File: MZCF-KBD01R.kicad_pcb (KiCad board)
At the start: 2 copper layers, 256.5 x 127.8 mm, 126 parts, among them CN2 XH-4AW_C2908613, SW1 SW_Push, SW10 SW_Push, SW11 SW_Push, SW12 SW_Push, SW13 SW_Push, SW14 SW_Push, SW15 SW_Push, SW16 SW_Push, SW17 SW_Push, SW18 SW_Push, SW19 SW_Push, SW2 SW_Push, SW20 SW_Push, SW21 SW_Push, SW22 SW_Push, SW23 SW_Push, SW24 SW_Push, SW25 SW_Push, SW26 SW_Push, SW27 SW_Push, SW28 SW_Push, SW29 SW_Push, SW3 SW_Push, SW30 SW_Push, SW31 SW_Push, SW32 SW_Push, SW33 SW_Push, SW34 SW_Push, SW35 SW_Push, SW36 SW_Push, SW37 SW_Push, SW38 SW_Push, SW39 SW_Push, SW4 SW_Push, SW40 SW_Push, SW41 SW_Push, SW42 SW_Push, SW43 SW_Push, SW44 SW_Push, SW45 SW_Push, SW46 SW_Push, SW47 SW_Push, SW48 SW_Push, SW49 SW_Push, SW5 SW_Push, SW50 SW_Push, SW51 SW_Push, SW52 SW_Push, SW53 SW_Push, SW55 SW_Push, SW56 SW_Push, SW6 SW_Push, SW7 SW_Push, SW8 SW_Push, SW9 SW_Push, U1 RP2040-ZERO

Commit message: feat: add hotswap MX switches and PCB stabilizer support
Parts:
- removed CN2: XH-4AW_C2908613, lcsc_footprints:C2908613_CONN-TH_XH-4AW
- removed D1, D12, D24, D35, D36, D40, D53, D55, D56: 1N4148W, ComboDiode
- removed the H1 at (22.4, 21.3)
- removed H10, H11, H12, H13, H2, H3, H4, H5, H6, H7, H8, H9: MountingHole_2.2mm_M2, MountingHole:MountingHole_2.2mm_M2
- removed SW1, SW12, SW24, SW35, SW36, SW40, SW53, SW55, SW56: SW_Push, MX
- added CN1: PJ-320A_C49284721, lcsc_footprints:C49284721_AUDIO-TH_PJ-320A_C49284721, B.Cu at (109.2, 28.5)
- added D54: 1N4148W, ComboDiode, B.Cu at (204.8, 140.3)
- added H1: MountingHole_2.2mm_M2, MountingHole:MountingHole_2.2mm_M2, F.Cu at (205.1, 116.2)
- added H1: MountingHole_2.2mm_M2, MountingHole:MountingHole_2.2mm_M2, F.Cu at (142.9, 87.0)
- added H1: MountingHole_2.2mm_M2, MountingHole:MountingHole_2.2mm_M2, F.Cu at (86.4, 134.0)
- added H1: MountingHole_2.2mm_M2, MountingHole:MountingHole_2.2mm_M2, F.Cu at (186.7, 44.5)
- added H1: MountingHole_2.2mm_M2, MountingHole:MountingHole_2.2mm_M2, F.Cu at (190.5, 76.2)
- added H1: MountingHole_2.2mm_M2, MountingHole:MountingHole_2.2mm_M2, F.Cu at (149.2, 142.9)
- added H1: MountingHole_2.2mm_M2, MountingHole:MountingHole_2.2mm_M2, F.Cu at (47.6, 22.9)
- added H1: MountingHole_2.2mm_M2, MountingHole:MountingHole_2.2mm_M2, F.Cu at (38.1, 67.9)
- added H1: MountingHole_2.2mm_M2, MountingHole:MountingHole_2.2mm_M2, F.Cu at (95.2, 67.9)
- added H1: MountingHole_2.2mm_M2, MountingHole:MountingHole_2.2mm_M2, F.Cu at (125.1, 44.5)
- added H1: MountingHole_2.2mm_M2, MountingHole:MountingHole_2.2mm_M2, F.Cu at (213.6, 21.6)
- added H1: MountingHole_2.2mm_M2, MountingHole:MountingHole_2.2mm_M2, F.Cu at (45.7, 144.1)
- added H1: MountingHole_2.2mm_M2, MountingHole:MountingHole_2.2mm_M2, F.Cu at (38.1, 44.5)
- added ST1: , STAB_MX, F.Cu at (171.4, 59.1)
- added ST2: , STAB_MX, F.Cu at (169.1, 97.2)
- added ST3: , STAB_MX, B.Cu at (157.2, 116.2)
- added ST4: , STAB_MX, F.Cu at (64.3, 135.3)
- added SW54: SW_Push, MX, F.Cu at (204.8, 135.3)
- moved D7 188.2 mm to (38.1, 35.5), turned to 0 degrees
- moved SW7 188.2 mm to (38.1, 30.5)
- moved U1 164.5 mm to (201.3, 33.0)
- moved D14 159.6 mm to (66.7, 64.1), turned to 0 degrees
- moved SW14 159.6 mm to (66.7, 59.1)
- moved D21 157.7 mm to (95.2, 83.1), turned to 0 degrees
- moved SW21 157.7 mm to (95.2, 78.1)
- moved D42 143.7 mm to (166.7, 140.3), turned to 0 degrees
- moved SW42 143.7 mm to (166.7, 135.3)
- moved D28 132.1 mm to (119.1, 102.2), turned to 0 degrees
- moved SW28 132.1 mm to (119.1, 97.2)
- moved D13 122.4 mm to (57.1, 35.5), turned to 0 degrees
- moved SW13 122.4 mm to (57.1, 30.5)
- moved D20 99.3 mm to (85.7, 64.1), turned to 0 degrees
- moved SW20 99.3 mm to (85.7, 59.1)
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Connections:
- D10 pad 1: /ROW2 -> /ROW3
- D11 pad 1: /ROW3 -> /ROW4
- D13 pad 1: /ROW5 -> /ROW0
- D14 pad 1: /ROW6 -> /ROW1
- D15 pad 1: /ROW0 -> /ROW2
- D16 pad 1: /ROW1 -> /ROW3
- D17 pad 1: /ROW2 -> /ROW4
- D18 pad 1: /ROW3 -> /ROW5
- D19 pad 1: /ROW4 -> /ROW0
- D20 pad 1: /ROW5 -> /ROW1
- D21 pad 1: /ROW6 -> /ROW2
- D22 pad 1: /ROW0 -> /ROW3
- D23 pad 1: /ROW1 -> /ROW4
- D25 pad 1: /ROW3 -> /ROW0
- D26 pad 1: /ROW4 -> /ROW1
- D27 pad 1: /ROW5 -> /ROW2
- D28 pad 1: /ROW6 -> /ROW3
- D29 pad 1: /ROW0 -> /ROW4
- D30 pad 1: /ROW1 -> /ROW5
- D31 pad 1: /ROW2 -> /ROW0
- D32 pad 1: /ROW3 -> /ROW1
- D33 pad 1: /ROW4 -> /ROW2
- D34 pad 1: /ROW5 -> /ROW3
- D37 pad 1: /ROW1 -> /ROW0
- D38 pad 1: /ROW2 -> /ROW1
- D39 pad 1: /ROW3 -> /ROW2
- D41 pad 1: /ROW5 -> /ROW4
- D42 pad 1: /ROW6 -> /ROW5
- D49 pad 1: /ROW6 -> /ROW0
- D50 pad 1: /ROW0 -> /ROW1
- D51 pad 1: /ROW1 -> /ROW2
- D52 pad 1: /ROW2 -> /ROW3
- D7 pad 1: /ROW6 -> /ROW0
- D8 pad 1: /ROW0 -> /ROW1
- D9 pad 1: /ROW1 -> /ROW2
- SW13 pad 1: /COL1 -> /COL2
- SW14 pad 1: /COL1 -> /COL2
- SW19 pad 1: /COL2 -> /COL3
- SW20 pad 1: /COL2 -> /COL3
- SW21 pad 1: /COL2 -> /COL3
- SW25 pad 1: /COL3 -> /COL4
- SW26 pad 1: /COL3 -> /COL4
- SW27 pad 1: /COL3 -> /COL4
- SW28 pad 1: /COL3 -> /COL4
- SW31 pad 1: /COL4 -> /COL5
- SW32 pad 1: /COL4 -> /COL5
- SW33 pad 1: /COL4 -> /COL5
- SW34 pad 1: /COL4 -> /COL5
- SW37 pad 1: /COL5 -> /COL6
- SW38 pad 1: /COL5 -> /COL6
- SW39 pad 1: /COL5 -> /COL6
- SW41 pad 1: /COL5 -> /COL6
- SW42 pad 1: /COL5 -> /COL6
- SW43 pad 1: /COL6 -> /COL7
- SW44 pad 1: /COL6 -> /COL7
- SW45 pad 1: /COL6 -> /COL7
- SW46 pad 1: /COL6 -> /COL7
- SW47 pad 1: /COL6 -> /COL7
- SW48 pad 1: /COL6 -> /COL7
- SW49 pad 1: /COL6 -> /COL8
- SW50 pad 1: /COL7 -> /COL8
- SW51 pad 1: /COL7 -> /COL8
- SW52 pad 1: /COL7 -> /COL8
- SW7 pad 1: /COL0 -> /COL1
- U1 pad 10: /ROW1 -> /ROW0
- U1 pad 11: /ROW2 -> /ROW1
- U1 pad 12: /ROW3 -> /ROW2
- U1 pad 13: /ROW4 -> /ROW3
- U1 pad 14: /ROW5 -> /ROW4
- U1 pad 15: /ROW6 -> /ROW5
- U1 pad 17: unconnected-(U1-GP26-Pad17) -> Net-(U1-GP26)
- U1 pad 18: unconnected-(U1-GP27-Pad18) -> Net-(U1-GP27)
- U1 pad 9: /ROW0 -> /COL8
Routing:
- net /ROW6: track 460.9 -> 0.00 mm, vias 1 -> 0
- net /COL5: track 561.0 -> 161.7 mm, vias 1 -> 0
- net /COL6: track 569.8 -> 186.5 mm, vias 1 -> 0
- net /COL7: track 509.1 -> 180.1 mm, vias 1 -> 0
- net /COL4: track 547.8 -> 235.3 mm, vias 2 -> 0
- net /COL3: track 542.7 -> 232.7 mm, vias 1 -> 0
- net /COL2: track 540.2 -> 273.7 mm, vias 2 -> 0
- net /COL8: track 0.00 -> 121.1 mm
- net /COL0: track 390.7 -> 296.6 mm, vias 1 -> 0
- net /COL1: track 353.7 -> 267.5 mm, vias 2 -> 0
- net /ROW5: track 358.7 -> 275.0 mm, vias 1 -> 0
- net Net-(U1-5V): track 85.4 -> 149.6 mm, vias 0 -> 1
- net /ROW4: track 317.9 -> 266.3 mm, vias 1 -> 2
- net Net-(U1-GP29): track 91.5 -> 142.4 mm
- net Net-(U1-GND): track 93.8 -> 144.4 mm, vias 0 -> 1
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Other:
- board size 256.5 x 127.8 mm -> 197.3 x 127.8 mm
- board text added: "MZCF-KBD01R V1 Rev.2"
- board text removed: "MZCF-KBD01R V1 Rev.1"

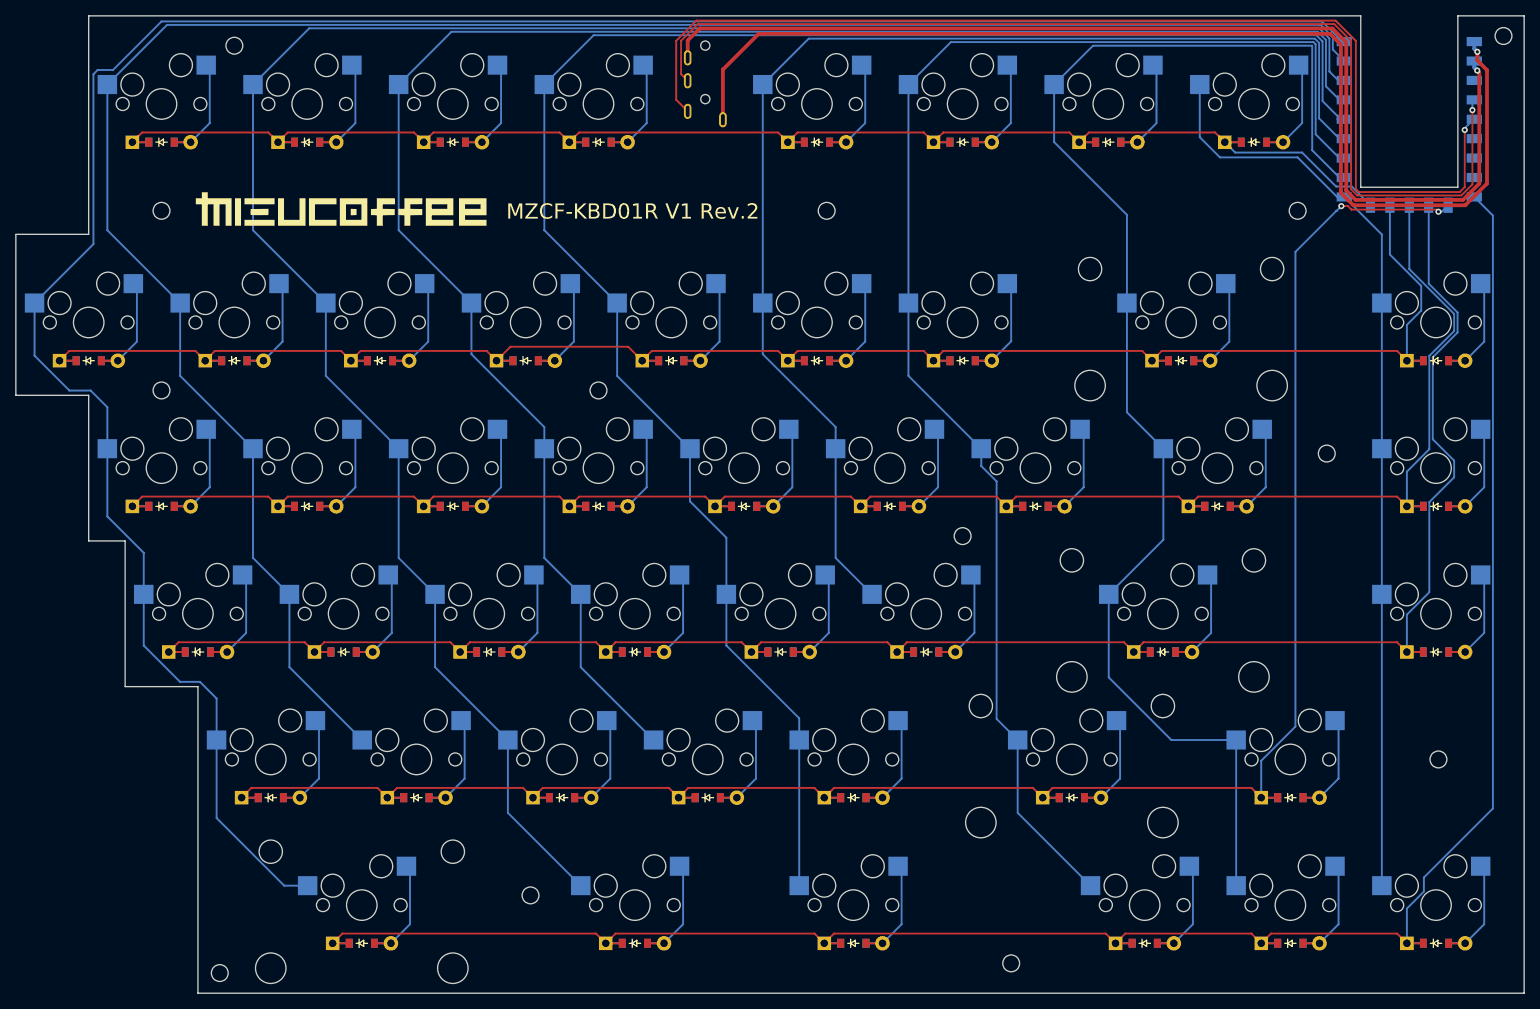
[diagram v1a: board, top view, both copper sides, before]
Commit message: fix(pcb): add controller cutouts and mating-edge clearance
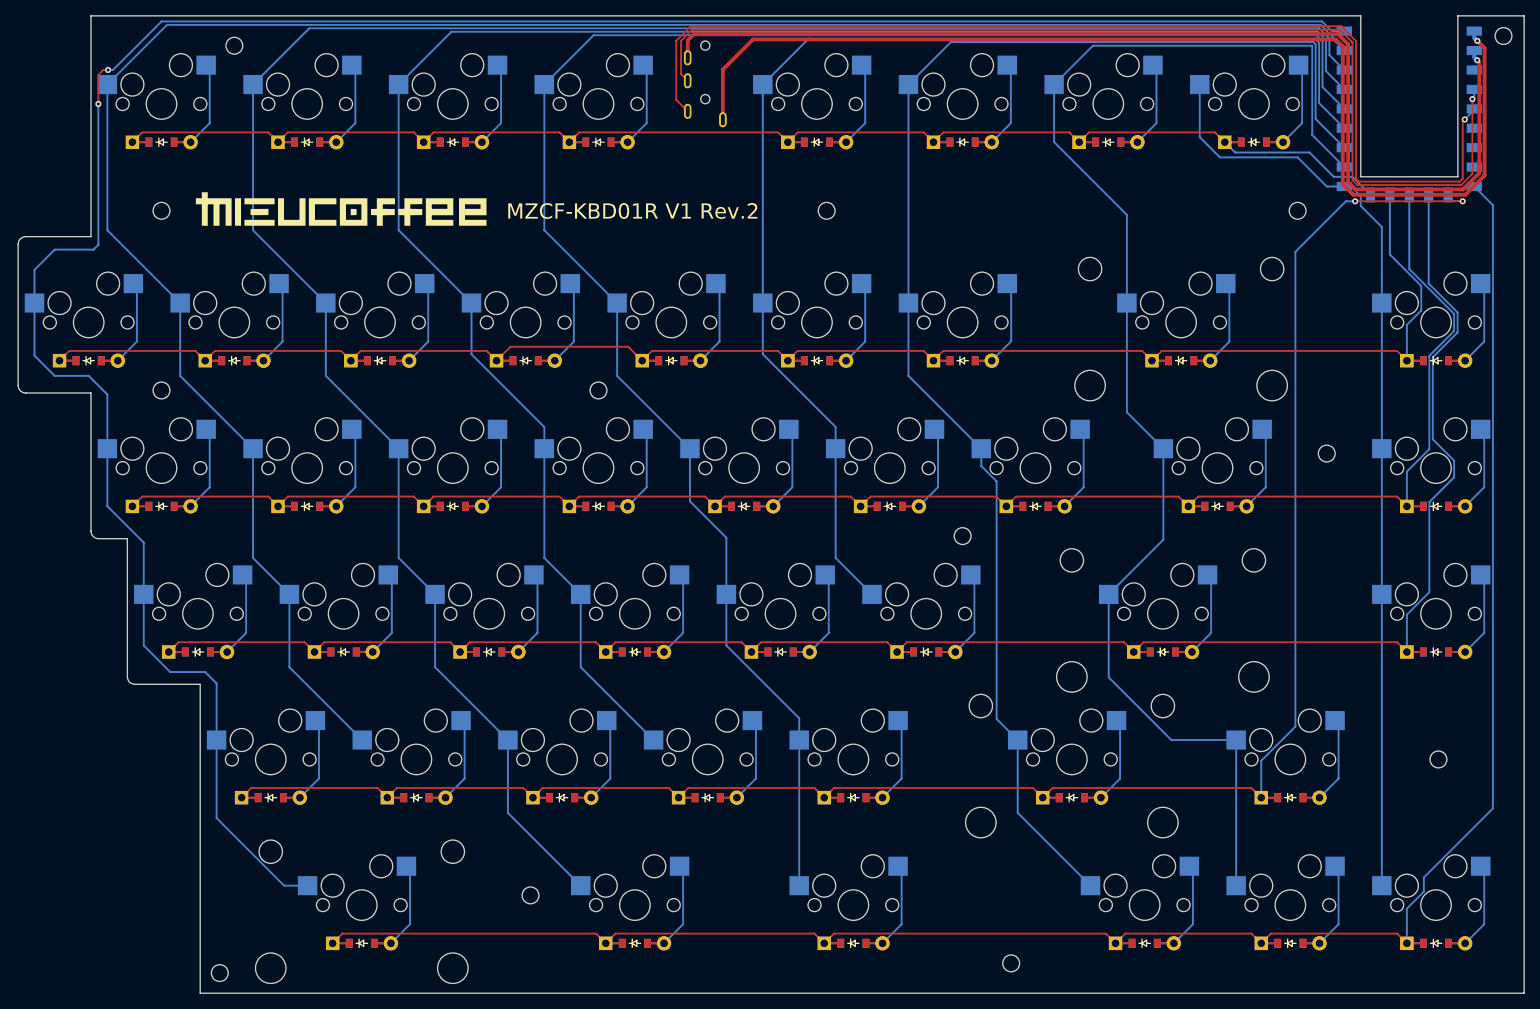
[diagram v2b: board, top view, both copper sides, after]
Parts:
- moved U1 1.37 mm to (201.3, 31.7)
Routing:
- net /COL0: track 296.6 -> 300.7 mm, vias 0 -> 2
- net /ROW4: track 266.3 -> 270.2 mm
- net Net-(U1-5V): track 149.6 -> 147.3 mm
- net Net-(U1-GND): track 144.4 -> 142.3 mm
- net Net-(U1-GP29): track 142.4 -> 140.4 mm
- net /COL4: track 235.3 -> 233.4 mm
- net /COL2: track 273.7 -> 271.8 mm
- net Net-(U1-GP28): track 144.4 -> 142.7 mm
- net /ROW5: track 275.0 -> 276.4 mm
- net /ROW3: track 269.0 -> 270.3 mm
- net /ROW2: track 258.4 -> 259.8 mm
- net /ROW1: track 247.8 -> 249.2 mm
- net /COL1: track 267.5 -> 266.1 mm
- net /COL8: track 121.1 -> 122.4 mm
- net /COL7: track 180.1 -> 179.0 mm
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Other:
- board size 197.3 x 127.8 mm -> 197 x 127.8 mm
